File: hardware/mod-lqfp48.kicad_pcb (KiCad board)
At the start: 2 copper layers, 2 parts, among them J1 Target, U1 STM32F103C8Tx

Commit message: mod-lqfp48 board WIP
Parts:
- added C1: 22pF, Capacitor_SMD:C_0805_2012Metric_Pad1.15x1.40mm_HandSolder, F.Cu at (102.2, 94.6)
- added C2: 22pF, Capacitor_SMD:C_0805_2012Metric_Pad1.15x1.40mm_HandSolder, F.Cu at (102.9, 97.2)
- added C3: 100nF, Capacitor_SMD:C_0805_2012Metric_Pad1.15x1.40mm_HandSolder, F.Cu at (86.4, 90.9)
- added C4: 100nF, Capacitor_SMD:C_0805_2012Metric_Pad1.15x1.40mm_HandSolder, F.Cu at (94.0, 97.8)
- added C5: 100nF, Capacitor_SMD:C_0805_2012Metric_Pad1.15x1.40mm_HandSolder, F.Cu at (95.5, 90.2)
- added C6: 100nF, Capacitor_SMD:C_0805_2012Metric_Pad1.15x1.40mm_HandSolder, F.Cu at (89.9, 98.4)
- added JP1: SolderJumper_3_Open, Jumper:SolderJumper-3_P2.0mm_Open_TrianglePad1.0x1.5mm, F.Cu at (98.4, 92.1)
- added JP2: SolderJumper_2_Open, Jumper:SolderJumper-2_P1.3mm_Open_TrianglePad1.0x1.5mm, F.Cu at (98.4, 96.5)
- added Y1: 8MHz, Crystal:Crystal_HC18-U_Vertical, F.Cu at (104.1, 94.0)
- U1: moved to B.Cu
- moved U1 7.60 mm to (91.9, 96.4), turned to 90 degrees
- moved J1 2.29 mm to (83.8, 101.6)
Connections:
- net /VCC renamed +3V3
- J1 pad 1: /USB_DM -> /TX
- J1 pad 10: /RX -> /USB_D-
- J1 pad 2: /USB_DP -> /RX
- J1 pad 7: /SWDIO -> /SWCLK
- J1 pad 8: /SWCLK -> /SWDIO
- J1 pad 9: /TX -> /USB_D+
- U1 pad 32: /USB_DM -> /USB_D-
- U1 pad 33: /USB_DP -> /USB_D+
- U1 pad 5: /CLK -> Net-(JP1-Pad2)
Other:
- board outline added: 30.5 x 15.2 mm

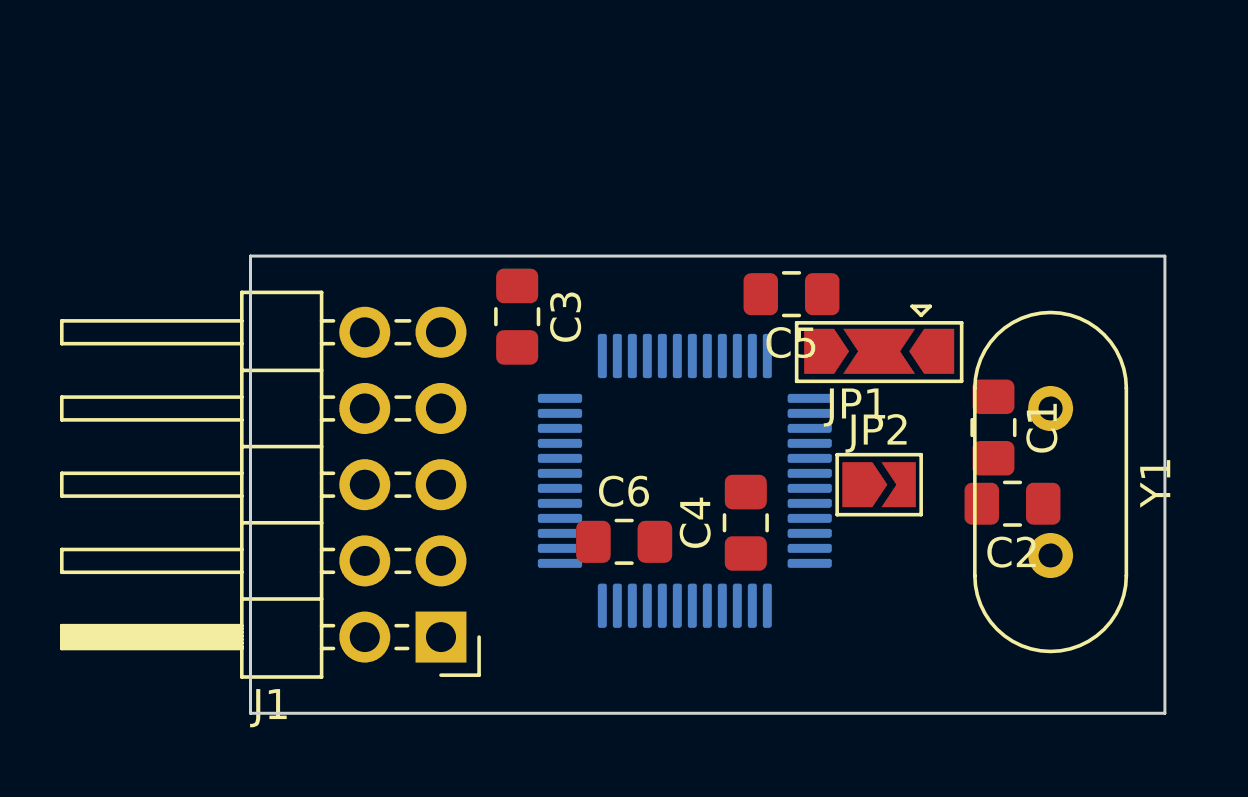
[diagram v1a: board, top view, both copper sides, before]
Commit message: mod-lqfp48 is finally routed
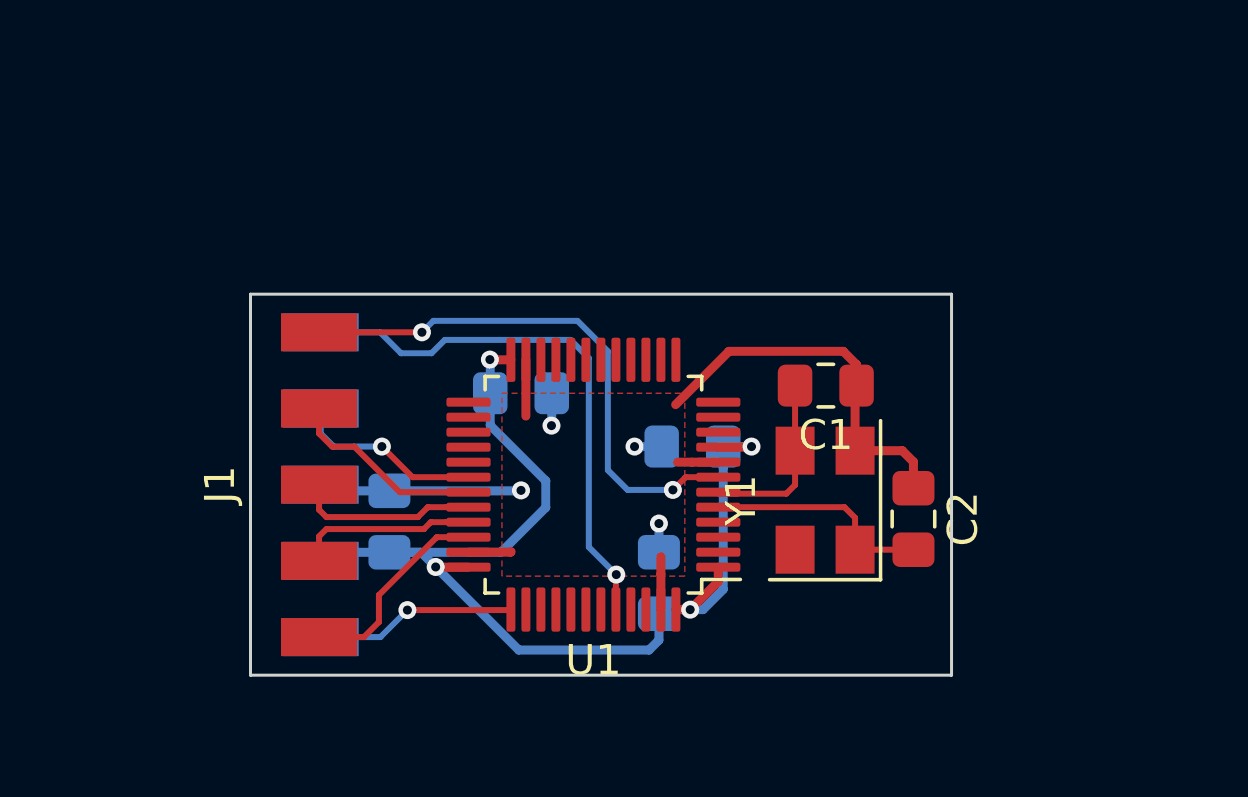
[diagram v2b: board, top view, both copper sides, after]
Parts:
- removed JP1: SolderJumper_3_Open, Jumper:SolderJumper-3_P2.0mm_Open_TrianglePad1.0x1.5mm
- removed JP2: SolderJumper_2_Open, Jumper:SolderJumper-2_P1.3mm_Open_TrianglePad1.0x1.5mm
- C1, C2: value 22pF -> 16pF
- C3, C4, C5, C6: moved to B.Cu
- J1: footprint Connector_PinHeader_2.54mm:PinHeader_2x05_P2.54mm_Horizontal -> unsorted:BH-10-Edge
- U1: moved to F.Cu
- Y1: footprint Crystal:Crystal_HC18-U_Vertical -> Crystal:Crystal_SMD_5032-4Pin_5.0x3.2mm
- moved C5 9.60 mm to (86.5, 93.5), turned to 0 degrees
- moved Y1 8.11 mm to (96.6, 97.0), turned to 90 degrees
- moved C6 7.85 mm to (82.1, 97.8), turned to 90 degrees
- moved C3 7.27 mm to (92.2, 95.2), turned to 180 degrees
- moved J1 6.51 mm to (79.8, 96.5), turned to 270 degrees
- moved C1 5.76 mm to (96.6, 93.2), turned to 180 degrees
- moved C4 3.52 mm to (91.1, 99.8)
- moved C2 3.34 mm to (99.6, 97.7), turned to 270 degrees
- moved U1 3.05 mm to (88.9, 96.5), turned to 180 degrees
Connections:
- C1 pad 1: Net-(C1-Pad1) -> GND
- C1 pad 2: GND -> Net-(C1-Pad2)
- C2 pad 1: Net-(C2-Pad1) -> GND
- C2 pad 2: GND -> Net-(C2-Pad2)
- J1 pad 1: /TX -> /NRST
- J1 pad 10: /USB_D- -> /SWCLK
- J1 pad 2: /RX -> /BOOT0
- J1 pad 3: +3V3 -> /RX
- J1 pad 4: GND -> /TX
- J1 pad 5: /NRST -> /USB_D-
- J1 pad 6: /CLK -> GND
- J1 pad 7: /SWCLK -> /USB_D+
- J1 pad 8: /SWDIO -> +3V3
- J1 pad 9: /USB_D+ -> /SWDIO
- U1 pad 44: GND -> /BOOT0
- U1 pad 5: Net-(JP1-Pad2) -> Net-(C2-Pad2)
- U1 pad 6: Net-(JP2-Pad1) -> Net-(C1-Pad2)
- Y1 pad 1: Net-(C1-Pad1) -> Net-(C2-Pad2)
- Y1 pad 2: Net-(C2-Pad1) -> GND
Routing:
- net +3V3: track 0.00 -> 38.7 mm, vias 0 -> 4
- net GND: track 0.00 -> 29.8 mm, vias 0 -> 4
- net /BOOT0: track 0.00 -> 18.4 mm, vias 0 -> 1
- net /NRST: track 0.00 -> 18.3 mm, vias 0 -> 2
- net Net-(C2-Pad2): track 0.00 -> 7.72 mm
- net /SWDIO: track 0.00 -> 6.89 mm
- net /SWCLK: track 0.00 -> 6.72 mm, vias 0 -> 1
- net /RX: track 0.00 -> 6.63 mm
- net /TX: track 0.00 -> 6.37 mm, vias 0 -> 1
- net /USB_D-: track 0.00 -> 6.05 mm
- net Net-(C1-Pad2): track 0.00 -> 6.03 mm
- net /USB_D+: track 0.00 -> 5.99 mm
- added copper zone on F.Cu, net GND
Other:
- board size 30.5 x 15.2 mm -> 23.4 x 12.7 mm
- net class Default: trace_width 0.25 -> 0.2; via_dia 0.8 -> 0.6; via_drill 0.4 -> 0.3
- net class Power added: clearance 0.2, trace_width 0.3, via_dia 0.6, via_drill 0.3
